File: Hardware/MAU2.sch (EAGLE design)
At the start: 28 parts, among them IC1 BMP280, P1 47346-0001, U1 MSP430F5507IRGZR

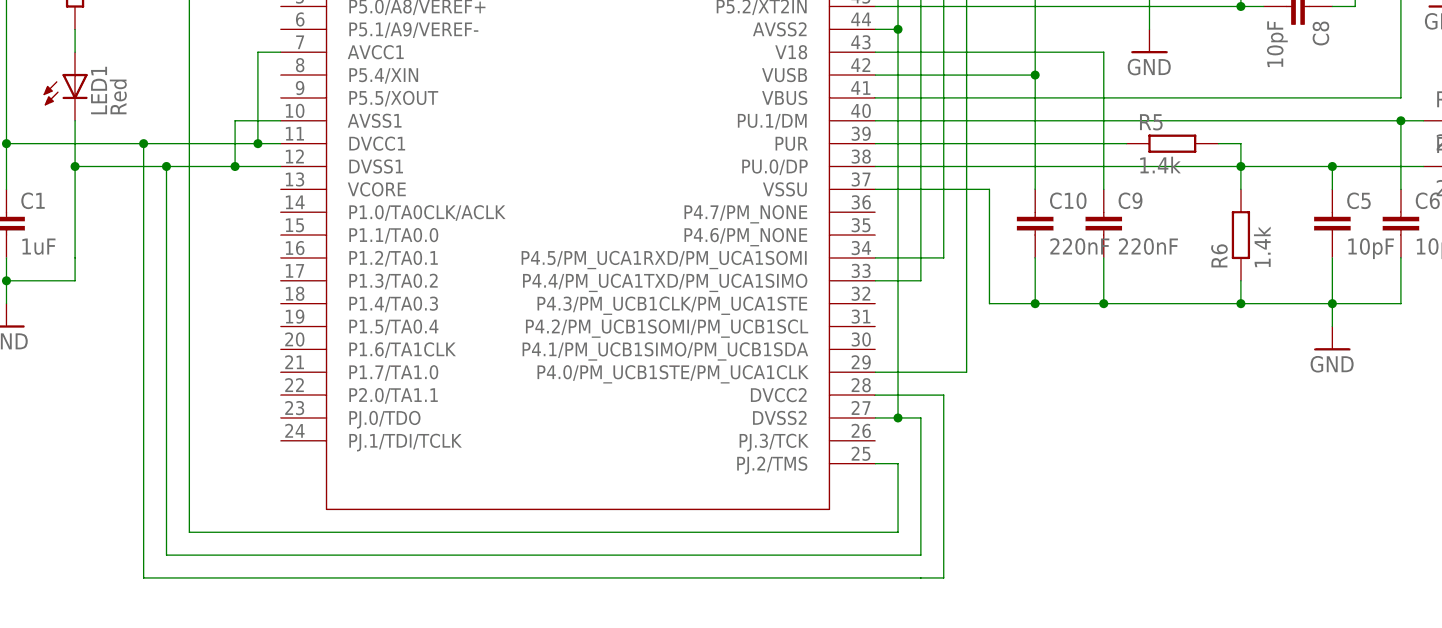
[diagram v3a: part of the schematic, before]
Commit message: All components positioned
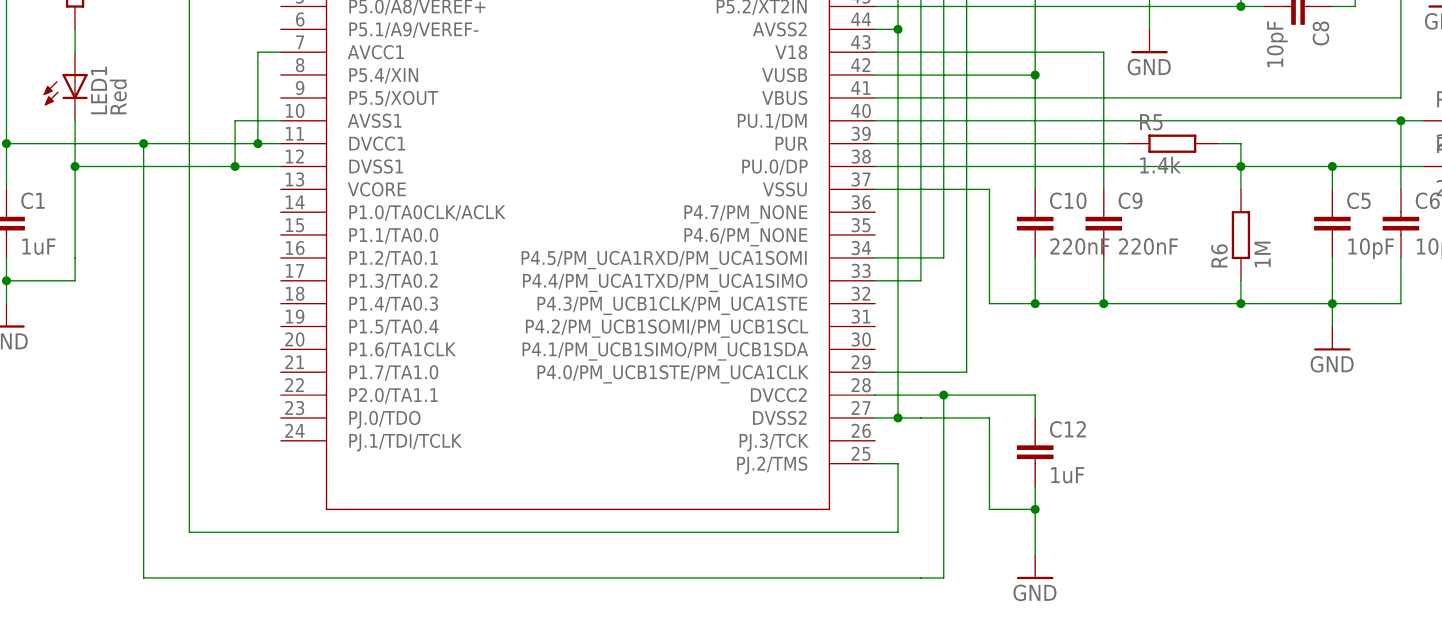
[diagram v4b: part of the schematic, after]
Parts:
- added C12: 1uF, rcl:C-EUC0201
- R6: value 1.4k -> 1M
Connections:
- net GND: now also C12.2
- net VCC-FET: now also C12.1
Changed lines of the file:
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@@
 <part name="GND1" library="supply1" library_urn="urn:adsk.eagle:library:371" deviceset="GND" device=""/>
 <part name="R5" library="rcl" library_urn="urn:adsk.eagle:library:334" deviceset="R-EU_" device="R0201" package3d_urn="urn:adsk.eagle:package:23593/1" value="1.4k"/>
-<part name="R6" library="rcl" library_urn="urn:adsk.eagle:library:334" deviceset="R-EU_" device="R0201" package3d_urn="urn:adsk.eagle:package:23593/1" value="1.4k"/>
+<part name="R6" library="rcl" library_urn="urn:adsk.eagle:library:334" deviceset="R-EU_" device="R0201" package3d_urn="urn:adsk.eagle:package:23593/1" value="1M"/>
 <part name="XTAL_24MHZ" library="GenericComponents" deviceset="XTAL" device=""/>
 <part name="C7" library="rcl" library_urn="urn:adsk.eagle:library:334" deviceset="C-EU" device="C0201" package3d_urn="urn:adsk.eagle:package:23690/2" value="10pF"/>
@@
 <part name="C11" library="rcl" library_urn="urn:adsk.eagle:library:334" deviceset="C-EU" device="C0201" package3d_urn="urn:adsk.eagle:package:23690/2" value="10nF"/>
 <part name="GND7" library="supply1" library_urn="urn:adsk.eagle:library:371" deviceset="GND" device=""/>
+<part name="C12" library="rcl" library_urn="urn:adsk.eagle:library:334" deviceset="C-EU" device="C0201" package3d_urn="urn:adsk.eagle:package:23690/2" value="1uF"/>
+<part name="GND8" library="supply1" library_urn="urn:adsk.eagle:library:371" deviceset="GND" device=""/>
 </parts>
 <sheets>
@@
 <instance part="C11" gate="G$1" x="104.14" y="45.72" rot="R90"/>
 <instance part="GND7" gate="1" x="111.76" y="33.02"/>
+<instance part="C12" gate="G$1" x="99.06" y="-10.16"/>
+<instance part="GND8" gate="1" x="99.06" y="-25.4"/>
 </instances>
 <busses>
@@
 <net name="GND" class="0">
 <segment>
+<pinref part="C1" gate="G$1" pin="2"/>
 <pinref part="GND4" gate="1" pin="GND"/>
-<pinref part="C1" gate="G$1" pin="2"/>
 <wire x1="-15.24" y1="5.08" x2="-15.24" y2="7.62" width="0.1524" layer="91"/>
 <wire x1="-15.24" y1="7.62" x2="-15.24" y2="10.16" width="0.1524" layer="91"/>
-<wire x1="-7.62" y1="10.16" x2="-7.62" y2="7.62" width="0.1524" layer="91"/>
-<wire x1="-7.62" y1="7.62" x2="-15.24" y2="7.62" width="0.1524" layer="91"/>
 <junction x="-15.24" y="7.62"/>
 <pinref part="U1" gate="A" pin="DVSS1"/>
 <wire x1="15.24" y1="20.32" x2="10.16" y2="20.32" width="0.1524" layer="91"/>
-<wire x1="10.16" y1="20.32" x2="2.54" y2="20.32" width="0.1524" layer="91"/>
-<wire x1="2.54" y1="20.32" x2="-7.62" y2="20.32" width="0.1524" layer="91"/>
-<wire x1="-7.62" y1="20.32" x2="-7.62" y2="10.16" width="0.1524" layer="91"/>
-<pinref part="U1" gate="A" pin="DVSS2"/>
-<wire x1="81.28" y1="-7.62" x2="83.82" y2="-7.62" width="0.1524" layer="91"/>
-<wire x1="83.82" y1="-7.62" x2="86.36" y2="-7.62" width="0.1524" layer="91"/>
-<wire x1="86.36" y1="-7.62" x2="86.36" y2="-22.86" width="0.1524" layer="91"/>
-<wire x1="86.36" y1="-22.86" x2="2.54" y2="-22.86" width="0.1524" layer="91"/>
-<wire x1="2.54" y1="-22.86" x2="2.54" y2="20.32" width="0.1524" layer="91"/>
-<junction x="2.54" y="20.32"/>
-<pinref part="LED1" gate="G$1" pin="C"/>
-<wire x1="-7.62" y1="25.4" x2="-7.62" y2="20.32" width="0.1524" layer="91"/>
-<junction x="-7.62" y="20.32"/>
 <pinref part="U1" gate="A" pin="AVSS1"/>
 <wire x1="15.24" y1="25.4" x2="10.16" y2="25.4" width="0.1524" layer="91"/>
 <wire x1="10.16" y1="25.4" x2="10.16" y2="20.32" width="0.1524" layer="91"/>
 <junction x="10.16" y="20.32"/>
-<pinref part="U1" gate="A" pin="AVSS2"/>
-<wire x1="81.28" y1="35.56" x2="83.82" y2="35.56" width="0.1524" layer="91"/>
-<wire x1="83.82" y1="35.56" x2="83.82" y2="-7.62" width="0.1524" layer="91"/>
-<junction x="83.82" y="-7.62"/>
-<pinref part="U1" gate="A" pin="EPAD"/>
-<wire x1="81.28" y1="48.26" x2="83.82" y2="48.26" width="0.1524" layer="91"/>
-<wire x1="83.82" y1="48.26" x2="83.82" y2="35.56" width="0.1524" layer="91"/>
-<junction x="83.82" y="35.56"/>
+<wire x1="10.16" y1="20.32" x2="2.54" y2="20.32" width="0.1524" layer="91"/>
+<wire x1="2.54" y1="20.32" x2="-7.62" y2="20.32" width="0.1524" layer="91"/>
+<pinref part="LED1" gate="G$1" pin="C"/>
+<wire x1="-7.62" y1="25.4" x2="-7.62" y2="20.32" width="0.1524" layer="91"/>
+<junction x="-7.62" y="20.32"/>
+<wire x1="-7.62" y1="20.32" x2="-7.62" y2="10.16" width="0.1524" layer="91"/>
+<wire x1="-7.62" y1="10.16" x2="-7.62" y2="7.62" width="0.1524" layer="91"/>
+<wire x1="-7.62" y1="7.62" x2="-15.24" y2="7.62" width="0.1524" layer="91"/>
 </segment>
 <segment>
@@
 <wire x1="109.22" y1="45.72" x2="111.76" y2="45.72" width="0.1524" layer="91"/>
 <wire x1="111.76" y1="45.72" x2="111.76" y2="35.56" width="0.1524" layer="91"/>
+</segment>
+<segment>
+<pinref part="U1" gate="A" pin="DVSS2"/>
+<wire x1="81.28" y1="-7.62" x2="83.82" y2="-7.62" width="0.1524" layer="91"/>
+<wire x1="83.82" y1="-7.62" x2="86.36" y2="-7.62" width="0.1524" layer="91"/>
+<pinref part="U1" gate="A" pin="AVSS2"/>
+<wire x1="81.28" y1="35.56" x2="83.82" y2="35.56" width="0.1524" layer="91"/>
+<wire x1="83.82" y1="35.56" x2="83.82" y2="-7.62" width="0.1524" layer="91"/>
+<junction x="83.82" y="-7.62"/>
+<pinref part="U1" gate="A" pin="EPAD"/>
+<wire x1="81.28" y1="48.26" x2="83.82" y2="48.26" width="0.1524" layer="91"/>
+<wire x1="83.82" y1="48.26" x2="83.82" y2="35.56" width="0.1524" layer="91"/>
+<junction x="83.82" y="35.56"/>
+<pinref part="C12" gate="G$1" pin="2"/>
+<wire x1="99.06" y1="-15.24" x2="99.06" y2="-17.78" width="0.1524" layer="91"/>
+<wire x1="99.06" y1="-17.78" x2="93.98" y2="-17.78" width="0.1524" layer="91"/>
+<wire x1="93.98" y1="-17.78" x2="93.98" y2="-7.62" width="0.1524" layer="91"/>
+<wire x1="93.98" y1="-7.62" x2="86.36" y2="-7.62" width="0.1524" layer="91"/>
+<pinref part="GND8" gate="1" pin="GND"/>
+<wire x1="99.06" y1="-22.86" x2="99.06" y2="-17.78" width="0.1524" layer="91"/>
+<junction x="99.06" y="-17.78"/>
 </segment>
 </net>
@@
 <wire x1="12.7" y1="33.02" x2="12.7" y2="22.86" width="0.1524" layer="91"/>
 <junction x="12.7" y="22.86"/>
-</segment>
-</net>
+<pinref part="C12" gate="G$1" pin="1"/>
+<wire x1="99.06" y1="-7.62" x2="99.06" y2="-5.08" width="0.1524" layer="91"/>
+<wire x1="99.06" y1="-5.08" x2="88.9" y2="-5.08" width="0.1524" layer="91"/>
+<junction x="88.9" y="-5.08"/>
+</segment>
+</net>

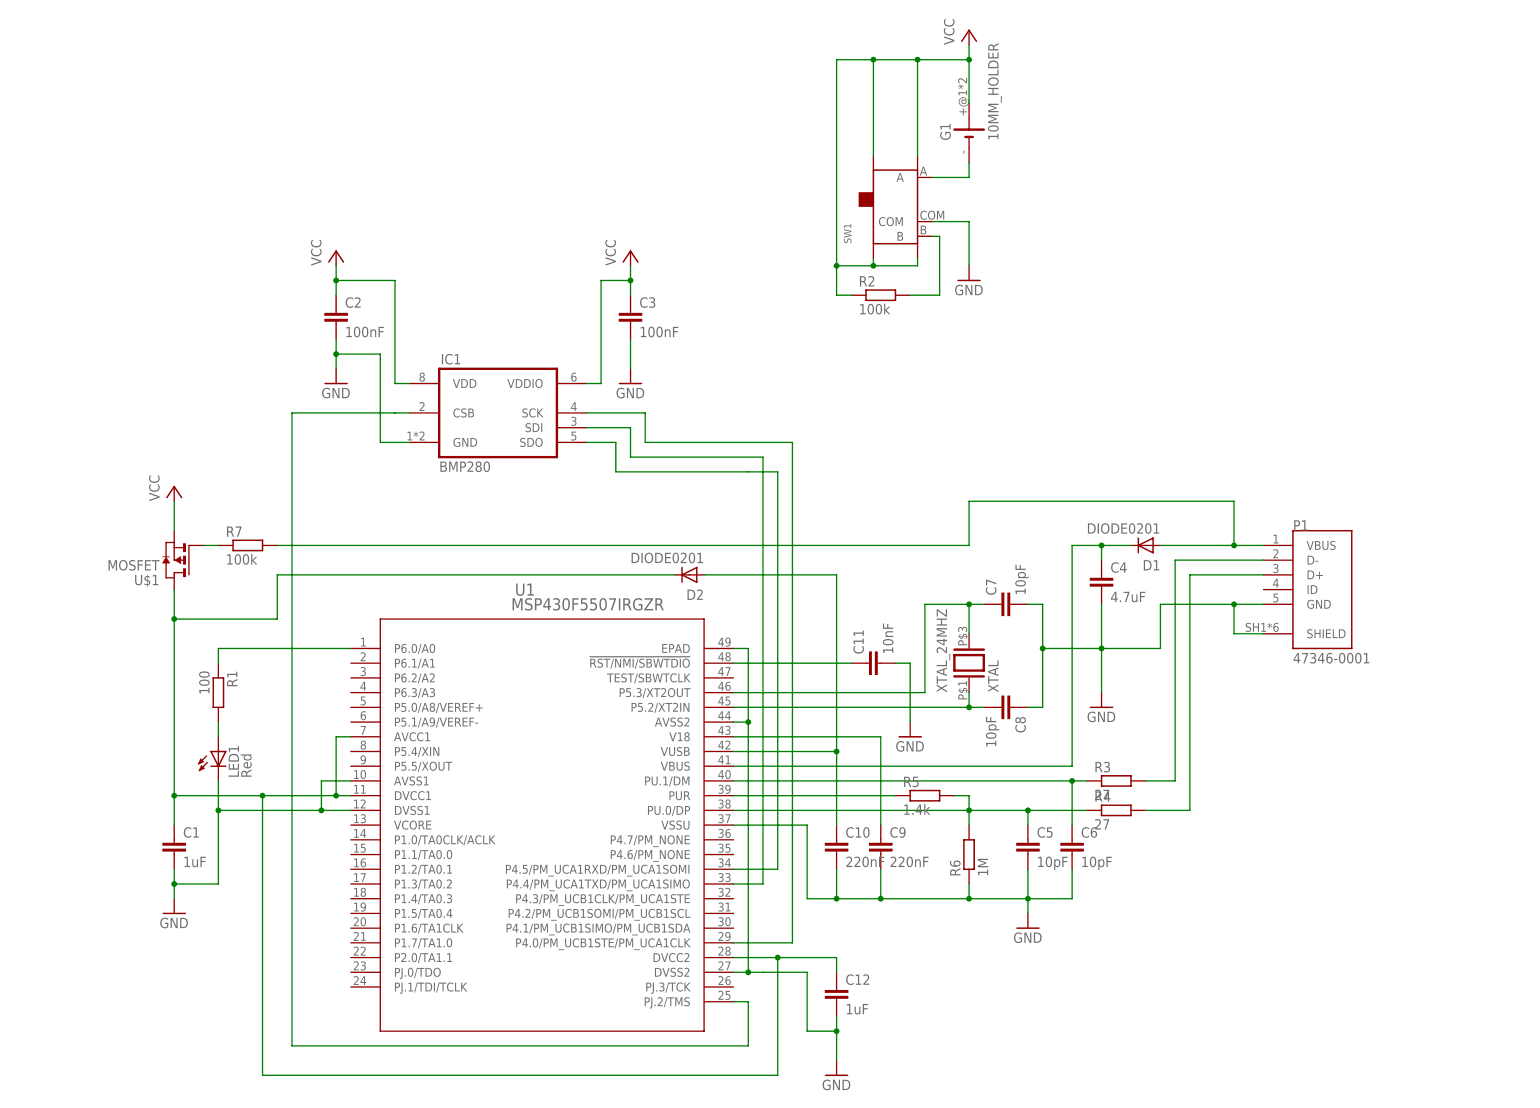
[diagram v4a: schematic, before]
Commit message: Routing in progress, set BMP280 supply to VCC-FET
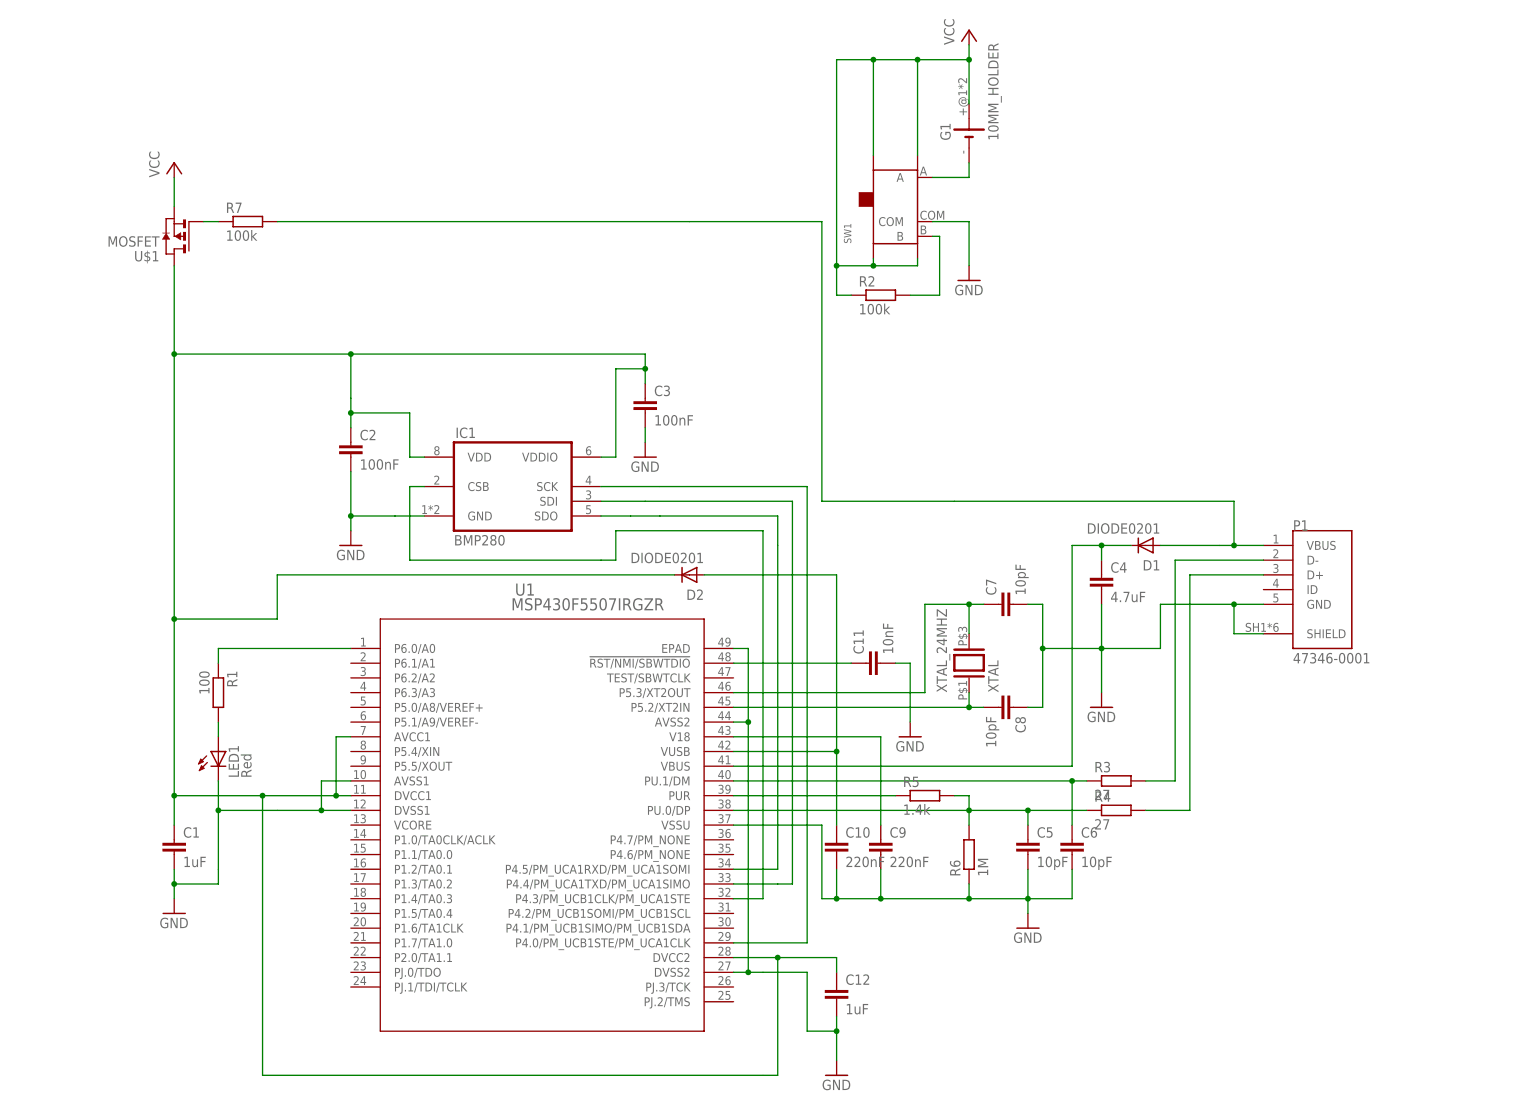
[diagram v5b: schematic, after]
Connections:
- net N$20: now also U1.P4.3/PM_UCB1CLK/PM_UCA1STE; no longer U1.PJ.2/TMS
- net VCC: no longer C2.1, C3.1, IC1.VDD, IC1.VDDIO
- net VCC-FET: now also C2.1, C3.1, IC1.VDD, IC1.VDDIO
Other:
- moved on the sheet: C2, C3, IC1, R7, U$1

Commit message: Finished routing
DVCC2 and RST capacitors removed.
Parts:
- removed C11: 10nF, rcl:C-EUC0201
- removed C12: 1uF, rcl:C-EUC0201
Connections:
- removed net N$17: C11.1, U1.!RST/NMI/SBWTDIO
- net GND: no longer C11.2, C12.2
- net VCC-FET: no longer C12.1
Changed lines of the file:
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@@
 <part name="R7" library="rcl" library_urn="urn:adsk.eagle:library:334" deviceset="R-EU_" device="R0201" package3d_urn="urn:adsk.eagle:package:23593/1" value="100k"/>
 <part name="D2" library="GenericComponents" deviceset="DIODE" device="0201"/>
-<part name="C11" library="rcl" library_urn="urn:adsk.eagle:library:334" deviceset="C-EU" device="C0201" package3d_urn="urn:adsk.eagle:package:23690/2" value="10nF"/>
-<part name="GND7" library="supply1" library_urn="urn:adsk.eagle:library:371" deviceset="GND" device=""/>
-<part name="C12" library="rcl" library_urn="urn:adsk.eagle:library:334" deviceset="C-EU" device="C0201" package3d_urn="urn:adsk.eagle:package:23690/2" value="1uF"/>
-<part name="GND8" library="supply1" library_urn="urn:adsk.eagle:library:371" deviceset="GND" device=""/>
 </parts>
 <sheets>
@@
 <instance part="R7" gate="G$1" x="-2.54" y="121.92"/>
 <instance part="D2" gate="G$1" x="73.66" y="60.96" rot="R180"/>
-<instance part="C11" gate="G$1" x="104.14" y="45.72" rot="R90"/>
-<instance part="GND7" gate="1" x="111.76" y="33.02"/>
-<instance part="C12" gate="G$1" x="99.06" y="-10.16"/>
-<instance part="GND8" gate="1" x="99.06" y="-25.4"/>
 </instances>
 <busses>
@@
 <wire x1="-7.62" y1="10.16" x2="-7.62" y2="7.62" width="0.1524" layer="91"/>
 <wire x1="-7.62" y1="7.62" x2="-15.24" y2="7.62" width="0.1524" layer="91"/>
+<pinref part="U1" gate="A" pin="DVSS2"/>
+<wire x1="81.28" y1="-7.62" x2="83.82" y2="-7.62" width="0.1524" layer="91"/>
+<pinref part="U1" gate="A" pin="AVSS2"/>
+<wire x1="81.28" y1="35.56" x2="83.82" y2="35.56" width="0.1524" layer="91"/>
+<wire x1="83.82" y1="35.56" x2="83.82" y2="-7.62" width="0.1524" layer="91"/>
+<pinref part="U1" gate="A" pin="EPAD"/>
+<wire x1="81.28" y1="48.26" x2="83.82" y2="48.26" width="0.1524" layer="91"/>
+<wire x1="83.82" y1="48.26" x2="83.82" y2="35.56" width="0.1524" layer="91"/>
+<junction x="83.82" y="35.56"/>
+<wire x1="83.82" y1="-7.62" x2="83.82" y2="-22.86" width="0.1524" layer="91"/>
+<wire x1="83.82" y1="-22.86" x2="10.16" y2="-22.86" width="0.1524" layer="91"/>
+<junction x="83.82" y="-7.62"/>
+<wire x1="10.16" y1="-22.86" x2="10.16" y2="20.32" width="0.1524" layer="91"/>
 </segment>
 <segment>
@@
 <junction x="106.68" y="5.08"/>
 <junction x="121.92" y="5.08"/>
-</segment>
-<segment>
-<pinref part="C11" gate="G$1" pin="2"/>
-<pinref part="GND7" gate="1" pin="GND"/>
-<wire x1="109.22" y1="45.72" x2="111.76" y2="45.72" width="0.1524" layer="91"/>
-<wire x1="111.76" y1="45.72" x2="111.76" y2="35.56" width="0.1524" layer="91"/>
-</segment>
-<segment>
-<pinref part="U1" gate="A" pin="DVSS2"/>
-<wire x1="81.28" y1="-7.62" x2="83.82" y2="-7.62" width="0.1524" layer="91"/>
-<wire x1="83.82" y1="-7.62" x2="86.36" y2="-7.62" width="0.1524" layer="91"/>
-<pinref part="U1" gate="A" pin="AVSS2"/>
-<wire x1="81.28" y1="35.56" x2="83.82" y2="35.56" width="0.1524" layer="91"/>
-<wire x1="83.82" y1="35.56" x2="83.82" y2="-7.62" width="0.1524" layer="91"/>
-<junction x="83.82" y="-7.62"/>
-<pinref part="U1" gate="A" pin="EPAD"/>
-<wire x1="81.28" y1="48.26" x2="83.82" y2="48.26" width="0.1524" layer="91"/>
-<wire x1="83.82" y1="48.26" x2="83.82" y2="35.56" width="0.1524" layer="91"/>
-<junction x="83.82" y="35.56"/>
-<pinref part="C12" gate="G$1" pin="2"/>
-<wire x1="99.06" y1="-15.24" x2="99.06" y2="-17.78" width="0.1524" layer="91"/>
-<wire x1="99.06" y1="-17.78" x2="93.98" y2="-17.78" width="0.1524" layer="91"/>
-<wire x1="93.98" y1="-17.78" x2="93.98" y2="-7.62" width="0.1524" layer="91"/>
-<wire x1="93.98" y1="-7.62" x2="86.36" y2="-7.62" width="0.1524" layer="91"/>
-<pinref part="GND8" gate="1" pin="GND"/>
-<wire x1="99.06" y1="-22.86" x2="99.06" y2="-17.78" width="0.1524" layer="91"/>
-<junction x="99.06" y="-17.78"/>
 </segment>
 </net>
@@
 <wire x1="12.7" y1="33.02" x2="12.7" y2="22.86" width="0.1524" layer="91"/>
 <junction x="12.7" y="22.86"/>
-<pinref part="C12" gate="G$1" pin="1"/>
-<wire x1="99.06" y1="-7.62" x2="99.06" y2="-5.08" width="0.1524" layer="91"/>
-<wire x1="99.06" y1="-5.08" x2="88.9" y2="-5.08" width="0.1524" layer="91"/>
-<junction x="88.9" y="-5.08"/>
 <pinref part="C3" gate="G$1" pin="1"/>
 <wire x1="66.04" y1="93.98" x2="66.04" y2="96.52" width="0.1524" layer="91"/>
@@
 </segment>
 </net>
-<net name="N$17" class="0">
-<segment>
-<pinref part="C11" gate="G$1" pin="1"/>
-<pinref part="U1" gate="A" pin="!RST/NMI/SBWTDIO"/>
-<wire x1="101.6" y1="45.72" x2="81.28" y2="45.72" width="0.1524" layer="91"/>
-</segment>
-</net>
